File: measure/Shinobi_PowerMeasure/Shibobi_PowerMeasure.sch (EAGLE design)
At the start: 50 parts, among them IC1 3.3V, T2 760390014, U1 SN6501DBVR, U2 TI-INA226

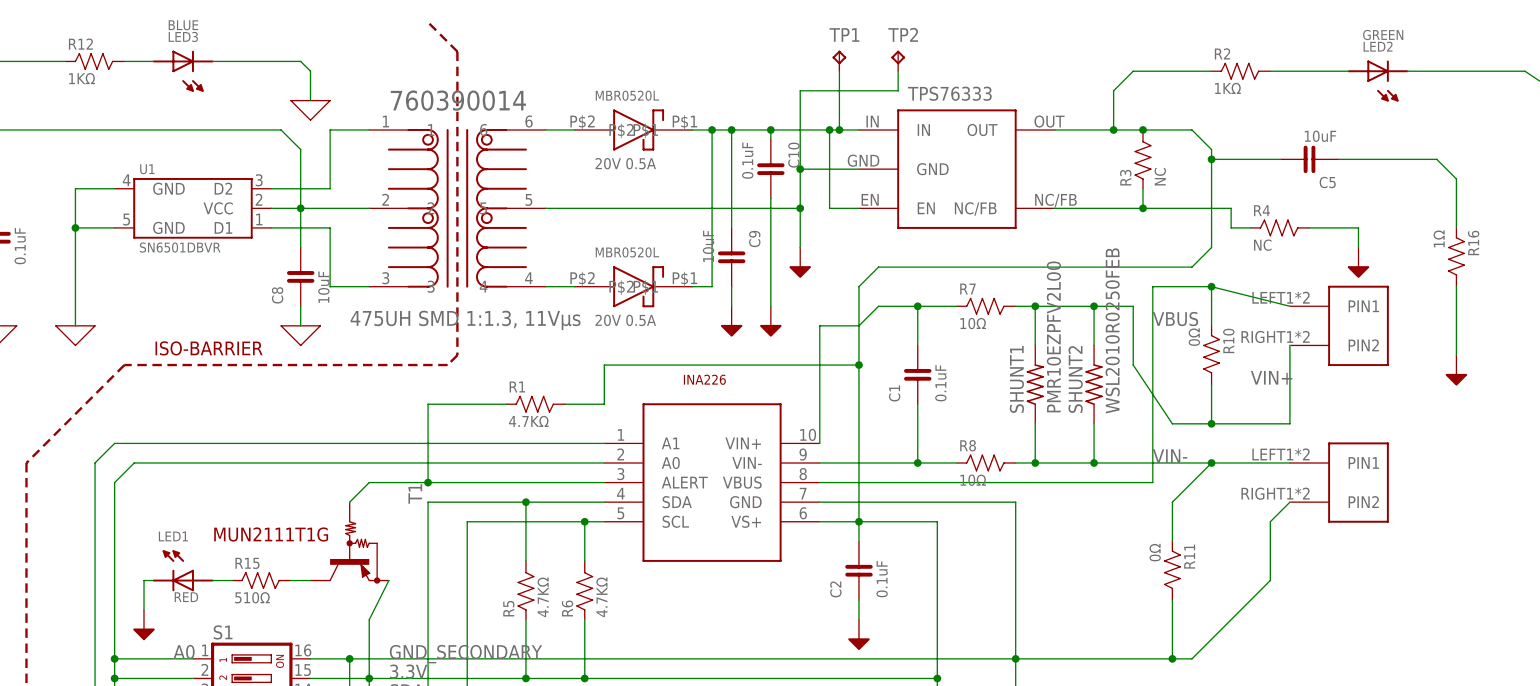
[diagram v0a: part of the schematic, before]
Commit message: Add silk printing Fixed garbled characters
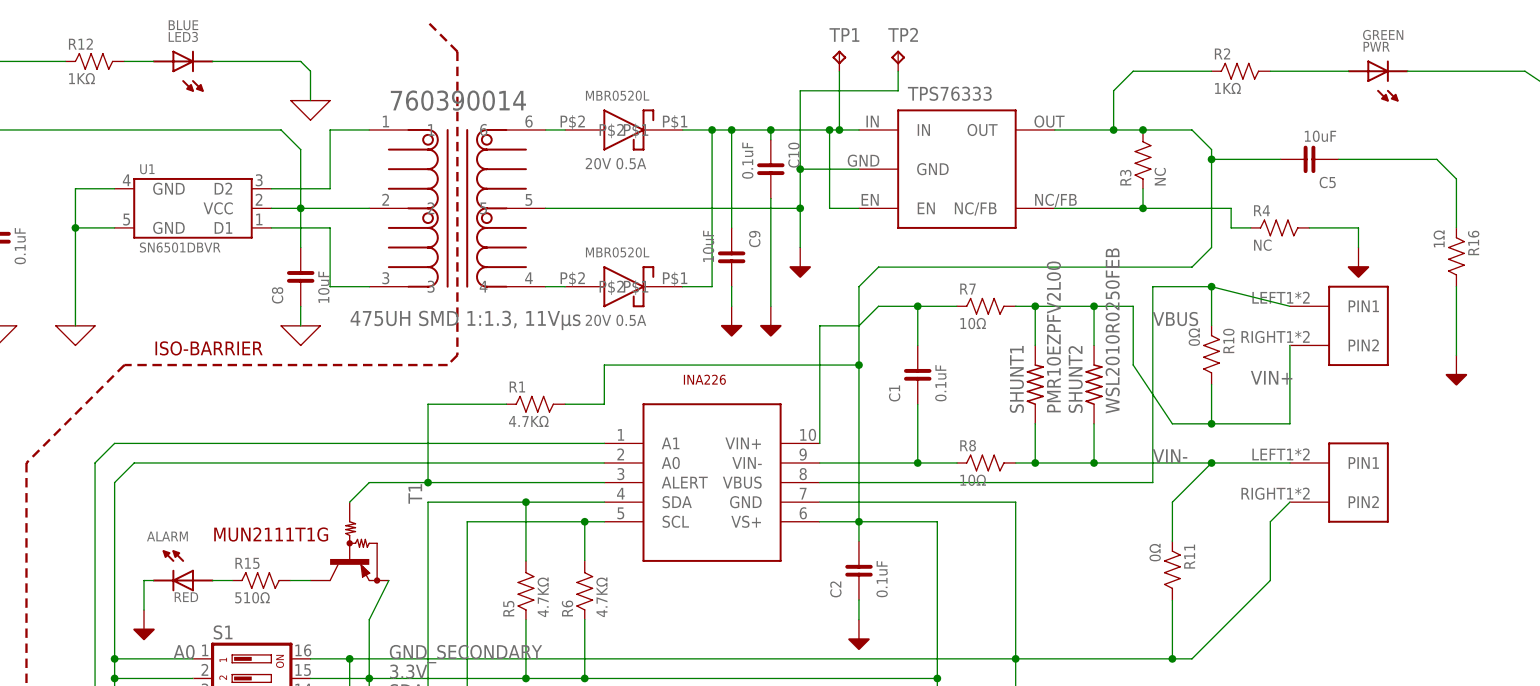
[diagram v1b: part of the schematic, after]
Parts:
- removed D1, D2: MBR0520L, FaBo:MBR0520L
- added U$12, U$7: MBR0520L, FaBo:MBR0520L
- renumbered ISO to U$18, LED1 to ALARM, LED2 to PWR, T2 to U$6
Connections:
- removed net N$15: D2.P$1, U$6.4
- new net N$6: U$6.6, U$7.P$1
- net N$14: now also U$12.P$1, U$6.4; no longer D1.P$1, U$6.6
- net N$16: now also U$12.P$2, U$7.P$2; no longer D1.P$2, D2.P$2
